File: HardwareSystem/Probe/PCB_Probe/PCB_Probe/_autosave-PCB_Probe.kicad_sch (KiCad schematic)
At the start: 24 parts, among them J1 Conn_01x15, J2 Conn_01x15, U1 TLC555xP, U2 LP2950CZ-3.0/NOPB

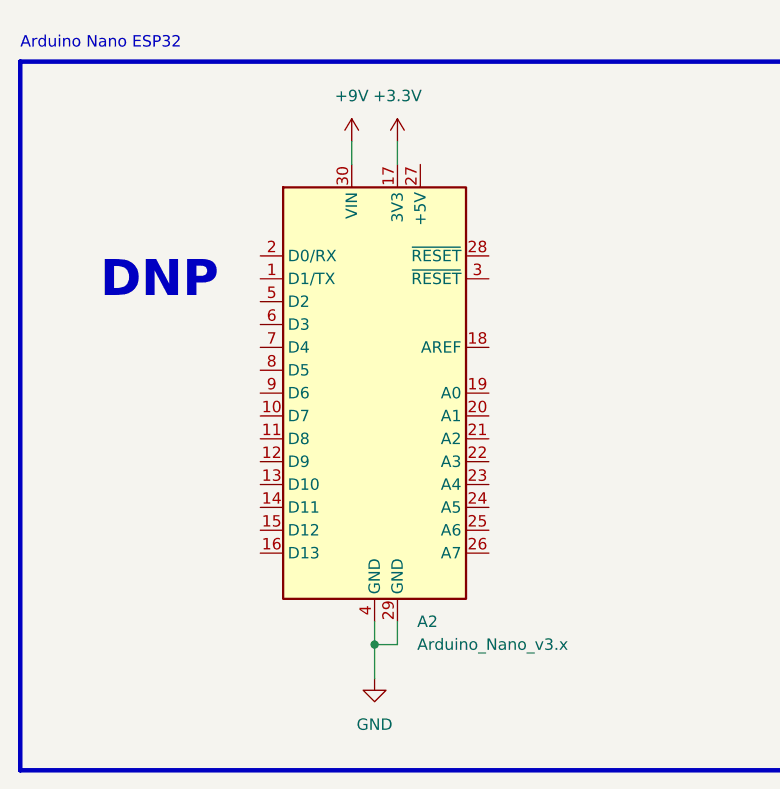
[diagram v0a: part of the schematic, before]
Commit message: more layout design
Added:
header footprint
pcb margins for probe
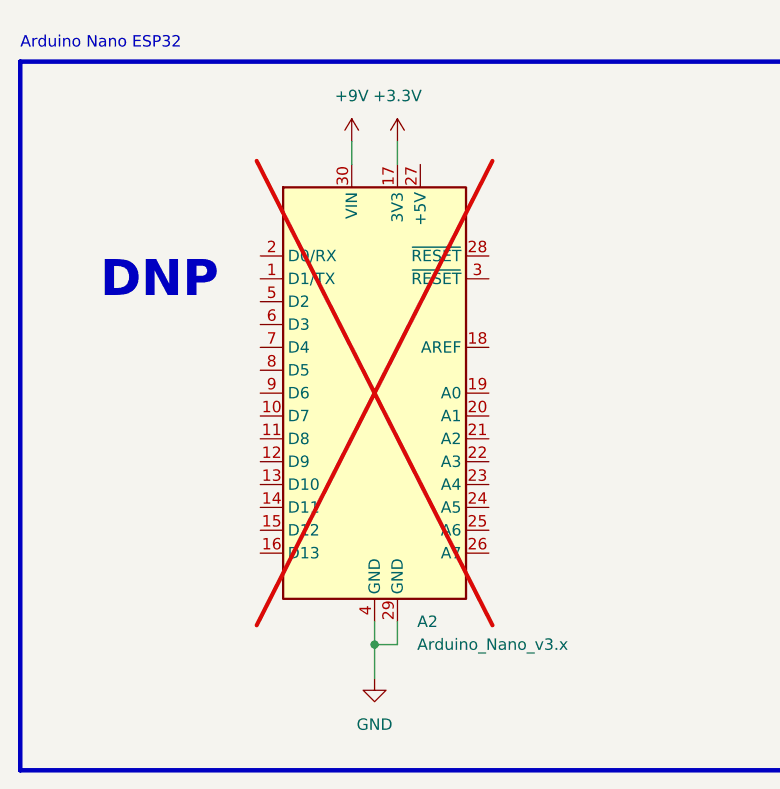
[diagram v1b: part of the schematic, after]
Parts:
- A2: now not fitted
- J2: footprint KiCADv6:PRT16279 -> Connector_PinSocket_1.00mm:PinSocket_1x15_P1.00mm_Vertical
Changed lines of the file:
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@@
       (effects (font (size 1.27 1.27)) (justify left))
     )
-    (property "Footprint" "KiCADv6:PRT16279" (at 165.1 48.26 0)
+    (property "Footprint" "Connector_PinSocket_1.00mm:PinSocket_1x15_P1.00mm_Vertical" (at 165.1 48.26 0)
       (effects (font (size 1.27 1.27)) hide)
     )
@@
   )
   (symbol (lib_id "MCU_Module:Arduino_Nano_v3.x") (at 66.04 57.15 0) (unit 1)
-    (in_bom yes) (on_board yes) (dnp no) (fields_autoplaced)
+    (in_bom yes) (on_board yes) (dnp yes) (fields_autoplaced)
     (property "Reference" "A2" (at 70.7741 82.55 0)
       (effects (font (size 1.27 1.27)) (justify left))
